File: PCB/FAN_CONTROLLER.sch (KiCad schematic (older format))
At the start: 3 parts

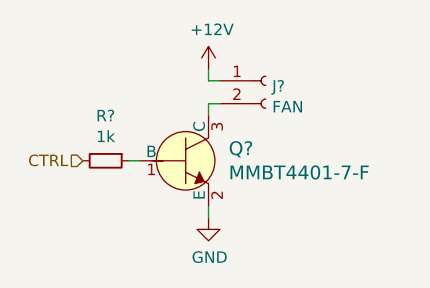
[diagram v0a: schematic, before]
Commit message: Added fan driver footprints
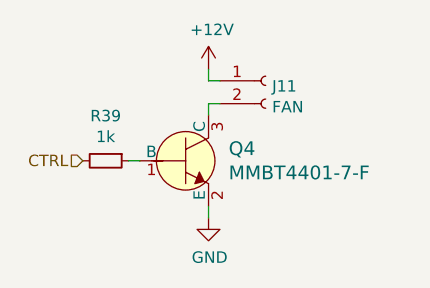
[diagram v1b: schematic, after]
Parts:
- J11: renamed from J?; footprint (none) -> Connector_Molex:Molex_KK-254_AE-6410-02A_1x02_P2.54mm_Vertical
- R39: renamed from R?; footprint (none) -> Resistor_SMD:R_0603_1608Metric
- gave numbers to parts that had none: 1
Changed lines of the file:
@@
 $EndDescr
 $Comp
-L Connector:Conn_01x02_Female J?
+L Connector:Conn_01x02_Female J11
 U 1 1 5E9765E9
 P 6350 3800
-F 0 "J?" H 6378 3776 50  0000 L CNN
+F 0 "J11" H 6378 3776 50  0000 L CNN
 F 1 "FAN" H 6378 3685 50  0000 L CNN
-F 2 "" H 6350 3800 50  0001 C CNN
+F 2 "Connector_Molex:Molex_KK-254_AE-6410-02A_1x02_P2.54mm_Vertical" H 6350 3800 50  0001 C CNN
 F 3 "~" H 6350 3800 50  0001 C CNN
 	1    6350 3800
@@
 $EndComp
 $Comp
-L dk_Transistors-Bipolar-BJT-Single:MMBT4401-7-F Q?
+L dk_Transistors-Bipolar-BJT-Single:MMBT4401-7-F Q4
 U 1 1 5E977513
 P 6000 4150
-F 0 "Q?" H 6188 4203 60  0000 L CNN
+F 0 "Q4" H 6188 4203 60  0000 L CNN
 F 1 "MMBT4401-7-F" H 6188 4097 60  0000 L CNN
 F 2 "digikey-footprints:SOT-23-3" H 6200 4350 60  0001 L CNN
@@
 	6100 3900 6150 3900
 $Comp
-L Device:R_Small R?
+L Device:R_Small R39
 U 1 1 5E978755
 P 5650 4150
-F 0 "R?" V 5454 4150 50  0000 C CNN
+F 0 "R39" V 5454 4150 50  0000 C CNN
 F 1 "1k" V 5545 4150 50  0000 C CNN
-F 2 "" H 5650 4150 50  0001 C CNN
+F 2 "Resistor_SMD:R_0603_1608Metric" H 5650 4150 50  0001 C CNN
 F 3 "~" H 5650 4150 50  0001 C CNN
 	1    5650 4150
@@
 	5750 4150 5800 4150
 $Comp
-L power:+12V #PWR?
+L power:+12V #PWR0101
 U 1 1 5E979D45
 P 6100 3750
-F 0 "#PWR?" H 6100 3600 50  0001 C CNN
+F 0 "#PWR0101" H 6100 3600 50  0001 C CNN
 F 1 "+12V" H 6115 3923 50  0000 C CNN
 F 2 "" H 6100 3750 50  0001 C CNN
@@
 	6100 3800 6150 3800
 $Comp
-L power:GND #PWR?
+L power:GND #PWR0154
 U 1 1 5E97A0B6
 P 6100 4400
-F 0 "#PWR?" H 6100 4150 50  0001 C CNN
+F 0 "#PWR0154" H 6100 4150 50  0001 C CNN
 F 1 "GND" H 6105 4227 50  0000 C CNN
 F 2 "" H 6100 4400 50  0001 C CNN
